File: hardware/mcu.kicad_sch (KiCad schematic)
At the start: 26 parts, among them SW1 BOOT / PTS810, SW2 RESET / PTS810, U2 ESP32-C6-MINI-1-H4, U4 BQ32000, Y1 32.768kHz

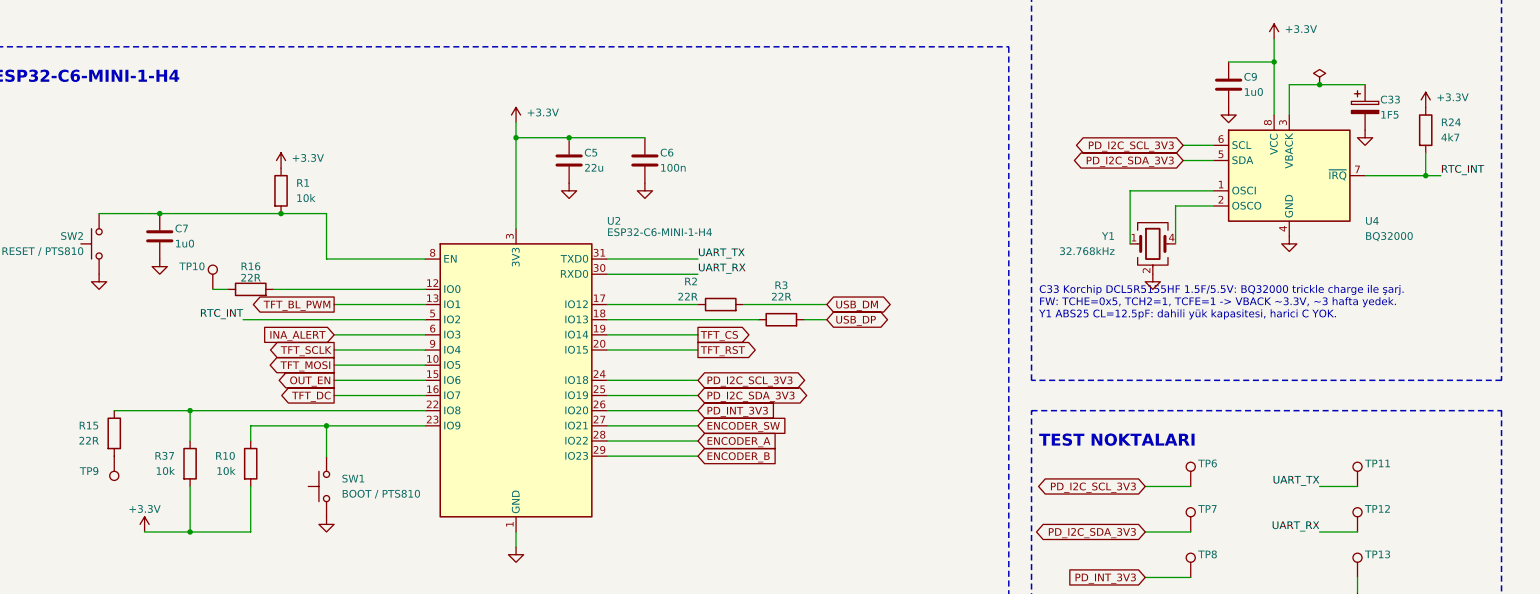
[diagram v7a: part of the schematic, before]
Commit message: hardware: R_Small_US, PD_INT bölücüsü, J4 lehim pedi ve Motorobit jaklar (TASK-043/044/045)
- Tüm dirençler Device:R -> Device:R_Small_US (21 sembol); netlist değişmedi.
- R8 12k / R9 20k -> R8 10k + R64 2k0 / R9 10k + R65 10k (oran 0.625,
  en kötü 2.73..3.34 V). BOM'dan 12k ve 20k kalktı.
- J4 DG142R klemens -> SolderWire-1.5sqmm 1x02 lehim pedi; J5/J6 ->
  Motorobit 4 mm banana (KOM.KNN.06.000021/22). Netlist değişmedi.
- Beklenen netlist farkı: PD_INT_3V3 = R64.2, R9.1, TP8.1, U2.26;
  Net-(R64-Pad1) = R8.2, R64.1; Net-(R65-Pad1) = R9.2, R65.1;
  GND'de R9.2 -> R65.2. ERC 0 hata / 0 uyarı.
- Takip: TASK-046/047 (jak numunesi), TASK-006/008'e AC eklendi.

Co-Authored-By: Claude Opus 5.5 <noreply@anthropic.com>
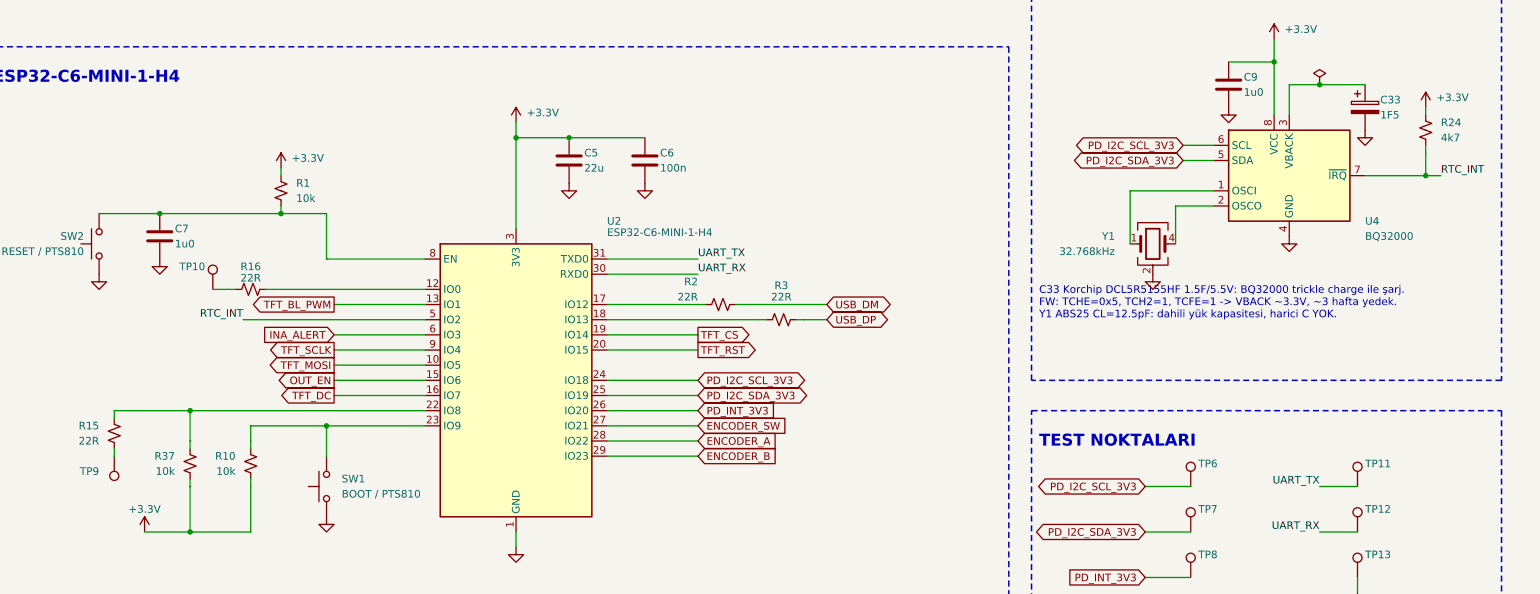
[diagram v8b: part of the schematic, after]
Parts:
- R1, R10, R15, R16, R2, R24, R3, R37: symbol Device:R -> Device:R_Small_US
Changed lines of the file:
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@@
 	)
 	(symbol
-		(lib_id "Device:R")
+		(lib_id "Device:R_Small_US")
 		(at 48.26 115.57 0)
 		(unit 1)
@@
 	)
 	(symbol
-		(lib_id "Device:R")
+		(lib_id "Device:R_Small_US")
 		(at 60.96 120.65 0)
 		(unit 1)
@@
 	)
 	(symbol
-		(lib_id "Device:R")
+		(lib_id "Device:R_Small_US")
 		(at 76.2 74.93 0)
 		(unit 1)
@@
 	)
 	(symbol
-		(lib_id "Device:R")
+		(lib_id "Device:R_Small_US")
 		(at 267.97 64.77 0)
 		(unit 1)
@@
 	)
 	(symbol
-		(lib_id "Device:R")
+		(lib_id "Device:R_Small_US")
 		(at 149.86 93.98 90)
 		(unit 1)
@@
 	)
 	(symbol
-		(lib_id "Device:R")
+		(lib_id "Device:R_Small_US")
 		(at 160.02 96.52 90)
 		(unit 1)
@@
 	)
 	(symbol
-		(lib_id "Device:R")
+		(lib_id "Device:R_Small_US")
 		(at 71.12 120.65 0)
 		(unit 1)
@@
 	)
 	(symbol
-		(lib_id "Device:R")
+		(lib_id "Device:R_Small_US")
 		(at 71.12 91.44 90)
 		(unit 1)
@@
 		)
 	)
+	(wire
+		(pts
+			(xy 48.26 113.03) (xy 48.26 111.76)
+		)
+		(stroke
+			(width 0)
+			(type default)
+		)
+	)
+	(wire
+		(pts
+			(xy 48.26 118.11) (xy 48.26 119.38)
+		)
+		(stroke
+			(width 0)
+			(type default)
+		)
+	)
+	(wire
+		(pts
+			(xy 60.96 118.11) (xy 60.96 116.84)
+		)
+		(stroke
+			(width 0)
+			(type default)
+		)
+	)
+	(wire
+		(pts
+			(xy 60.96 123.19) (xy 60.96 124.46)
+		)
+		(stroke
+			(width 0)
+			(type default)
+		)
+	)
+	(wire
+		(pts
+			(xy 76.2 72.39) (xy 76.2 71.12)
+		)
+		(stroke
+			(width 0)
+			(type default)
+		)
+	)
+	(wire
+		(pts
+			(xy 76.2 77.47) (xy 76.2 78.74)
+		)
+		(stroke
+			(width 0)
+			(type default)
+		)
+	)
+	(wire
+		(pts
+			(xy 267.97 62.23) (xy 267.97 60.96)
+		)
+		(stroke
+			(width 0)
+			(type default)
+		)
+	)
+	(wire
+		(pts
+			(xy 267.97 67.31) (xy 267.97 68.58)
+		)
+		(stroke
+			(width 0)
+			(type default)
+		)
+	)
+	(wire
+		(pts
+			(xy 147.32 93.98) (xy 146.05 93.98)
+		)
+		(stroke
+			(width 0)
+			(type default)
+		)
+	)
+	(wire
+		(pts
+			(xy 152.4 93.98) (xy 153.67 93.98)
+		)
+		(stroke
+			(width 0)
+			(type default)
+		)
+	)
+	(wire
+		(pts
+			(xy 157.48 96.52) (xy 156.21 96.52)
+		)
+		(stroke
+			(width 0)
+			(type default)
+		)
+	)
+	(wire
+		(pts
+			(xy 162.56 96.52) (xy 163.83 96.52)
+		)
+		(stroke
+			(width 0)
+			(type default)
+		)
+	)
+	(wire
+		(pts
+			(xy 71.12 118.11) (xy 71.12 116.84)
+		)
+		(stroke
+			(width 0)
+			(type default)
+		)
+	)
+	(wire
+		(pts
+			(xy 71.12 123.19) (xy 71.12 124.46)
+		)
+		(stroke
+			(width 0)
+			(type default)
+		)
+	)
+	(wire
+		(pts
+			(xy 68.58 91.44) (xy 67.31 91.44)
+		)
+		(stroke
+			(width 0)
+			(type default)
+		)
+	)
+	(wire
+		(pts
+			(xy 73.66 91.44) (xy 74.93 91.44)
+		)
+		(stroke
+			(width 0)
+			(type default)
+		)
+	)
